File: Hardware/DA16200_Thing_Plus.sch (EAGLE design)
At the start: 61 parts, among them J1 MICRO-SDFRICTION, J2 THING_PLUS, J3 Qwiic, J5 USB C, J6 microSD, J7 CORTEX_JTAG_DEBUG_PTH_NS, Q1 20V/4.2A/52mΩ/1.4W, U1 DA16200MOD, U2 CH340E_MSOP10, U3 MCP73831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

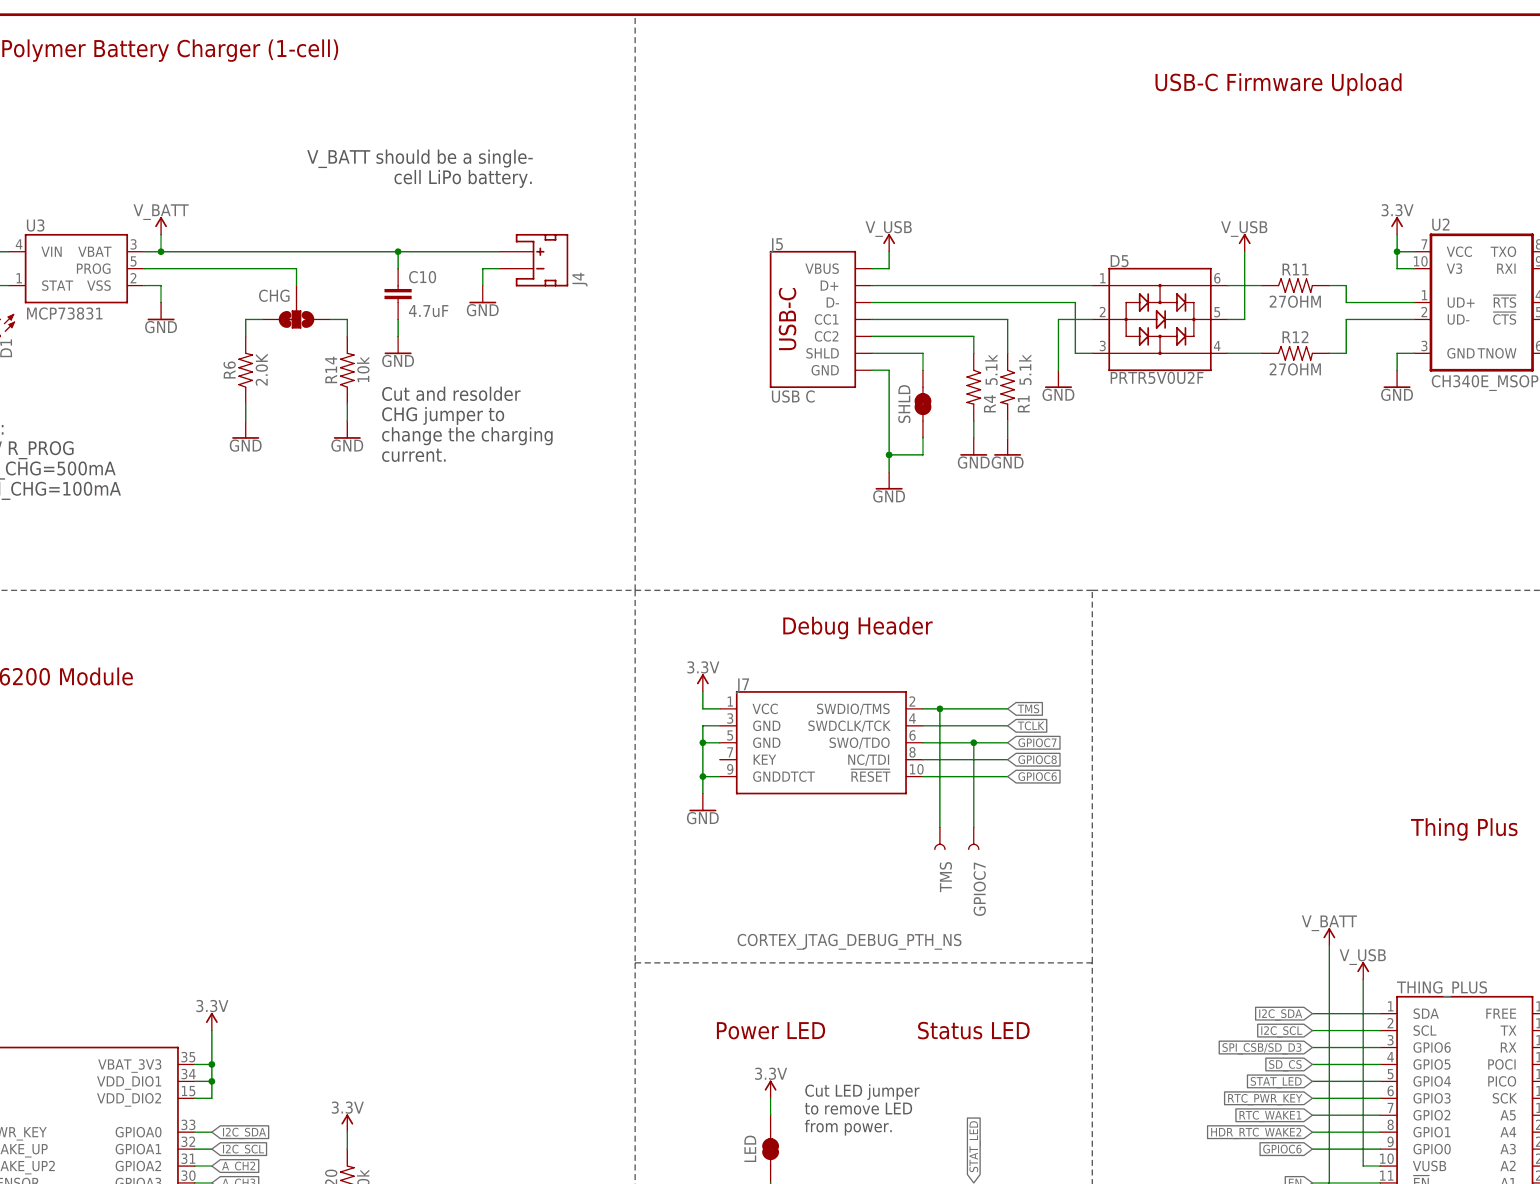
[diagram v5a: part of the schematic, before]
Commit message: Add jumper to remove 3.3V from CH340E
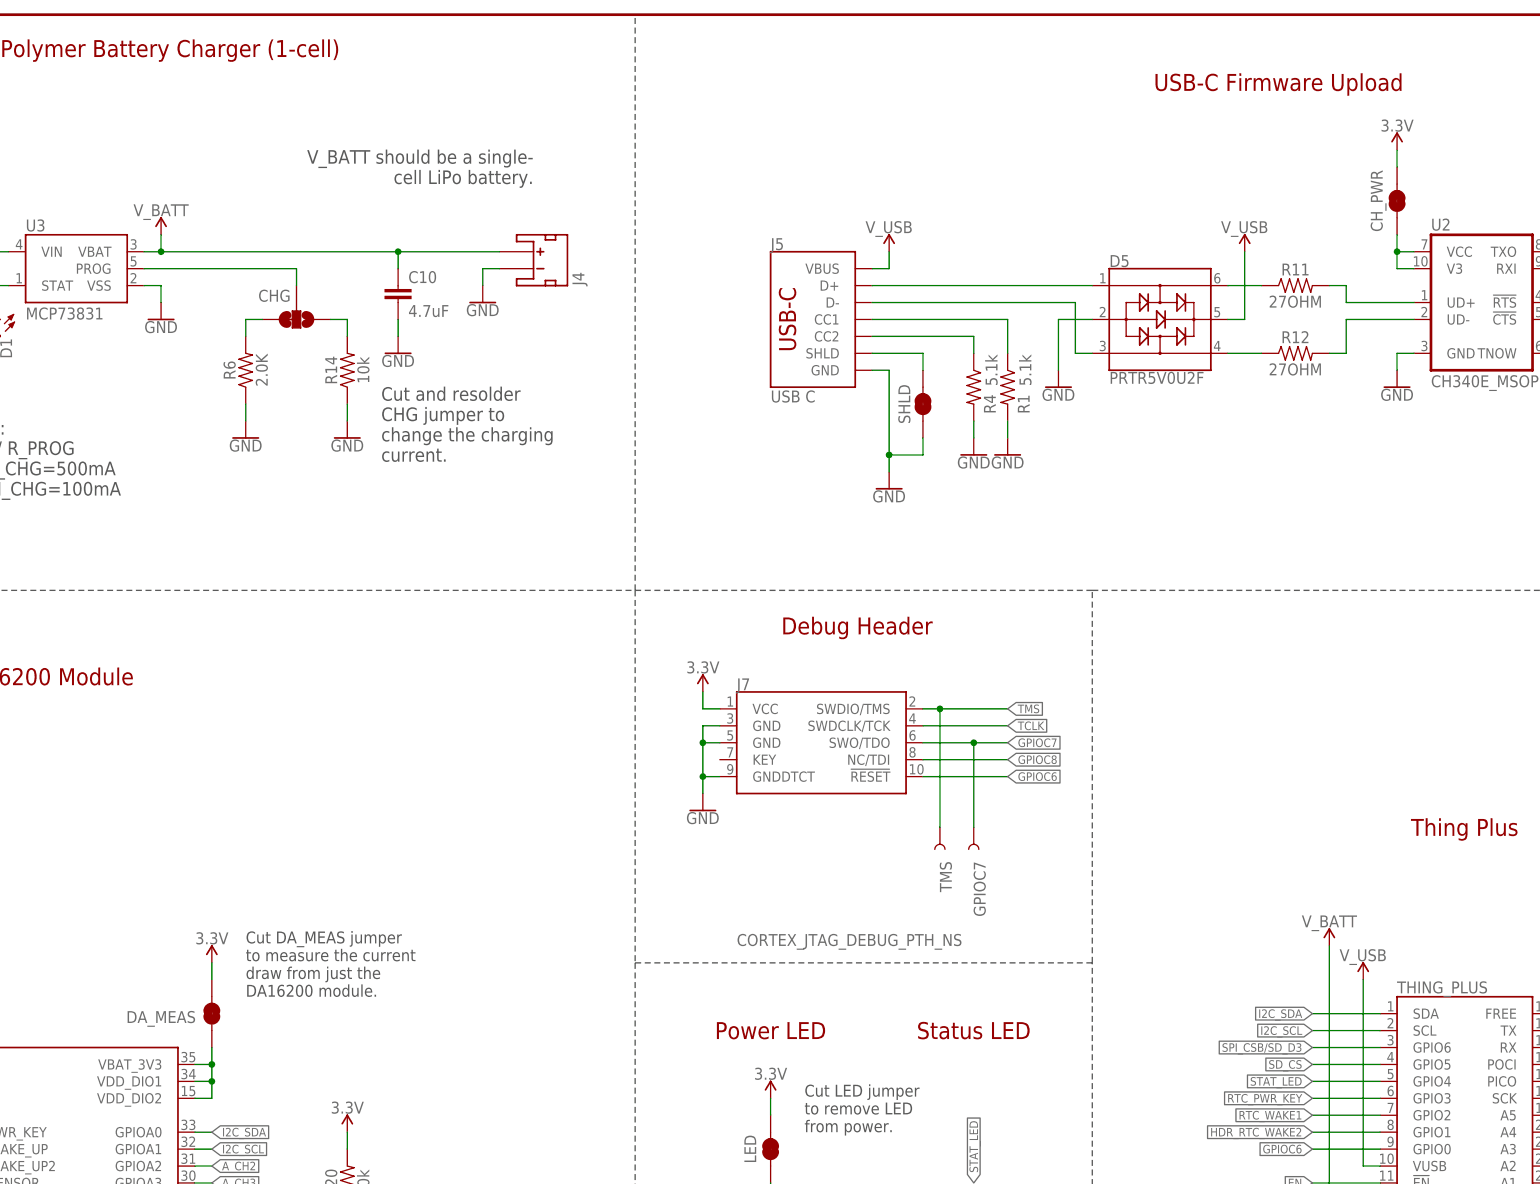
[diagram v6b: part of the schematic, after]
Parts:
- added CH_PWR, DA_MEAS: JUMPER-SMT_2_NC_TRACE_SILK, SparkFun-Jumpers:JUMPER-SMT_2_NC_TRACE_SILK
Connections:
- new net N$25: DA_MEAS.1, U1.VBAT_3V3, U1.VDD_DIO1, U1.VDD_DIO2
- new net N$26: CH_PWR.1, U2.V3, U2.VCC
- net 3.3V: now also CH_PWR.2, DA_MEAS.2; no longer U1.VBAT_3V3, U1.VDD_DIO1, U1.VDD_DIO2, U2.V3, U2.VCC
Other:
- note added: "Cut DA_MEAS jumper to measure the current draw from just the DA16200 module."
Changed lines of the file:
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@@
 <part name="J1" library="SparkFun-Connectors" deviceset="MICRO-SD" device="FRICTION"/>
 <part name="CHG_LED" library="SparkFun-Jumpers" deviceset="JUMPER-SMT_2_NC_TRACE" device="_SILK" package3d_urn="urn:adsk.eagle:package:39281/1"/>
+<part name="DA_MEAS" library="SparkFun-Jumpers" deviceset="JUMPER-SMT_2_NC_TRACE" device="_SILK" package3d_urn="urn:adsk.eagle:package:39281/1"/>
+<part name="CH_PWR" library="SparkFun-Jumpers" deviceset="JUMPER-SMT_2_NC_TRACE" device="_SILK" package3d_urn="urn:adsk.eagle:package:39281/1"/>
 </parts>
 <sheets>
@@
 to GND and enter sleep mode 1. Refer
 to the datasheet for more information.</text>
+<text x="203.2" y="132.08" size="1.778" layer="97" font="vector">Cut DA_MEAS jumper
+to measure the current
+draw from just the
+DA16200 module.</text>
 </plain>
 <instances>
@@
 <attribute name="VALUE" x="157.48" y="59.69" size="1.778" layer="96" align="top-left"/>
 </instance>
-<instance part="SUPPLY5" gate="G$1" x="198.12" y="127" smashed="yes">
-<attribute name="VALUE" x="198.12" y="129.794" size="1.778" layer="96" align="bottom-center"/>
+<instance part="SUPPLY5" gate="G$1" x="198.12" y="137.16" smashed="yes">
+<attribute name="VALUE" x="198.12" y="139.954" size="1.778" layer="96" align="bottom-center"/>
 </instance>
 <instance part="GND3" gate="1" x="198.12" y="55.88" smashed="yes">
@@
 <attribute name="VALUE" x="375.92" y="223.266" size="1.778" layer="96" align="top-center"/>
 </instance>
-<instance part="SUPPLY11" gate="G$1" x="375.92" y="246.38" smashed="yes">
-<attribute name="VALUE" x="375.92" y="249.174" size="1.778" layer="96" align="bottom-center"/>
+<instance part="SUPPLY11" gate="G$1" x="375.92" y="259.08" smashed="yes">
+<attribute name="VALUE" x="375.92" y="261.874" size="1.778" layer="96" align="bottom-center"/>
 </instance>
 <instance part="C1" gate="G$1" x="421.64" y="236.22" smashed="yes">
@@
 <instance part="CHG_LED" gate="G$1" x="147.32" y="233.68" smashed="yes" rot="R90">
 <attribute name="NAME" x="144.272" y="233.68" size="1.778" layer="95" font="vector" rot="R90" align="center"/>
+</instance>
+<instance part="DA_MEAS" gate="G$1" x="198.12" y="129.54" smashed="yes" rot="R90">
+<attribute name="NAME" x="190.5" y="129.032" size="1.778" layer="95" font="vector" rot="R180" align="center"/>
+</instance>
+<instance part="CH_PWR" gate="G$1" x="375.92" y="251.46" smashed="yes" rot="R90">
+<attribute name="NAME" x="372.872" y="251.46" size="1.778" layer="95" font="vector" rot="R90" align="center"/>
 </instance>
 </instances>
@@
 </segment>
 <segment>
-<pinref part="U1" gate="G$1" pin="VDD_DIO2"/>
-<wire x1="195.58" y1="116.84" x2="198.12" y2="116.84" width="0.1524" layer="91"/>
-<wire x1="198.12" y1="116.84" x2="198.12" y2="119.38" width="0.1524" layer="91"/>
-<pinref part="U1" gate="G$1" pin="VBAT_3V3"/>
-<wire x1="198.12" y1="119.38" x2="198.12" y2="121.92" width="0.1524" layer="91"/>
-<wire x1="198.12" y1="121.92" x2="198.12" y2="127" width="0.1524" layer="91"/>
-<wire x1="195.58" y1="121.92" x2="198.12" y2="121.92" width="0.1524" layer="91"/>
-<junction x="198.12" y="121.92"/>
-<pinref part="U1" gate="G$1" pin="VDD_DIO1"/>
-<wire x1="195.58" y1="119.38" x2="198.12" y2="119.38" width="0.1524" layer="91"/>
-<junction x="198.12" y="119.38"/>
-<pinref part="SUPPLY5" gate="G$1" pin="3.3V"/>
-</segment>
-<segment>
 <pinref part="J2" gate="G$1" pin="3V3"/>
 <wire x1="398.78" y1="93.98" x2="401.32" y2="93.98" width="0.1524" layer="91"/>
@@
 </segment>
 <segment>
-<pinref part="U2" gate="U1" pin="V3"/>
-<wire x1="378.46" y1="241.3" x2="375.92" y2="241.3" width="0.1524" layer="91"/>
-<wire x1="375.92" y1="241.3" x2="375.92" y2="243.84" width="0.1524" layer="91"/>
-<pinref part="U2" gate="U1" pin="VCC"/>
-<wire x1="375.92" y1="243.84" x2="375.92" y2="246.38" width="0.1524" layer="91"/>
-<wire x1="378.46" y1="243.84" x2="375.92" y2="243.84" width="0.1524" layer="91"/>
-<junction x="375.92" y="243.84"/>
-<pinref part="SUPPLY11" gate="G$1" pin="3.3V"/>
-</segment>
-<segment>
 <pinref part="C1" gate="G$1" pin="1"/>
 <pinref part="SUPPLY12" gate="G$1" pin="3.3V"/>
@@
 <wire x1="101.6" y1="58.42" x2="101.6" y2="60.96" width="0.1524" layer="91"/>
 <pinref part="SUPPLY2" gate="G$1" pin="3.3V"/>
+</segment>
+<segment>
+<pinref part="SUPPLY5" gate="G$1" pin="3.3V"/>
+<pinref part="DA_MEAS" gate="G$1" pin="2"/>
+<wire x1="198.12" y1="137.16" x2="198.12" y2="134.62" width="0.1524" layer="91"/>
+</segment>
+<segment>
+<pinref part="CH_PWR" gate="G$1" pin="2"/>
+<pinref part="SUPPLY11" gate="G$1" pin="3.3V"/>
+<wire x1="375.92" y1="256.54" x2="375.92" y2="259.08" width="0.1524" layer="91"/>
 </segment>
 </net>
@@
 </segment>
 </net>
+<net name="N$25" class="0">
+<segment>
+<pinref part="U1" gate="G$1" pin="VDD_DIO2"/>
+<wire x1="195.58" y1="116.84" x2="198.12" y2="116.84" width="0.1524" layer="91"/>
+<wire x1="198.12" y1="116.84" x2="198.12" y2="119.38" width="0.1524" layer="91"/>
+<pinref part="U1" gate="G$1" pin="VBAT_3V3"/>
+<wire x1="198.12" y1="119.38" x2="198.12" y2="121.92" width="0.1524" layer="91"/>
+<wire x1="195.58" y1="121.92" x2="198.12" y2="121.92" width="0.1524" layer="91"/>
+<pinref part="U1" gate="G$1" pin="VDD_DIO1"/>
+<wire x1="195.58" y1="119.38" x2="198.12" y2="119.38" width="0.1524" layer="91"/>
+<junction x="198.12" y="119.38"/>
+<pinref part="DA_MEAS" gate="G$1" pin="1"/>
+<wire x1="198.12" y1="124.46" x2="198.12" y2="121.92" width="0.1524" layer="91"/>
+<junction x="198.12" y="121.92"/>
+</segment>
+</net>
+<net name="N$26" class="0">
+<segment>
+<pinref part="U2" gate="U1" pin="V3"/>
+<wire x1="378.46" y1="241.3" x2="375.92" y2="241.3" width="0.1524" layer="91"/>
+<wire x1="375.92" y1="241.3" x2="375.92" y2="243.84" width="0.1524" layer="91"/>
+<pinref part="U2" gate="U1" pin="VCC"/>
+<wire x1="378.46" y1="243.84" x2="375.92" y2="243.84" width="0.1524" layer="91"/>
+<pinref part="CH_PWR" gate="G$1" pin="1"/>
+<wire x1="375.92" y1="246.38" x2="375.92" y2="243.84" width="0.1524" layer="91"/>
+<junction x="375.92" y="243.84"/>
+</segment>
+</net>

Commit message: Remove SD card socket from design
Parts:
- removed C2: 0.1uF, SparkFun-Capacitors:0.1UF-0402T-16V-10%
- removed J1: MICRO-SDFRICTION, SparkFun-Connectors:MICRO-SDFRICTION
- removed J6: microSD, SparkFun-Connectors:MICRO-SD-SDIOPUSH-PUSH
- removed R21: 10k, SparkFun-Resistors:10KOHM-0402T-1/16W-1%
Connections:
- removed net !RESET!/SPI_CLK/SD_D2: J1.DAT2, J2.!RESET, J2.SCK, J6.CLK/SCK, R13.2, U1.GPIOA7
- removed net SPI_CSB/SD_D3: J1.DAT3/!CS!, J2.GPIO6, R20.1, U1.GPIOA6
- removed net SPI_PICO/SD_D1: J1.DAT1, J2.PICO, J6.CMD/SDI, U1.GPIOA8
- removed net SPI_POCI/SD_D0: J1.DAT0/SDO, J2.POCI, J6.DAT0/SDO, U1.GPIOA9
- removed net U1RXI/SD_CLK: J1.CLK/SCK, J2.RX, U1.GPIOA5
- removed net U1TXO/SD_CMD: J1.CMD/SDI, J2.TX, U1.GPIOA4
- new net !RESET!/SPI_CLK: J2.!RESET, J2.SCK, R13.2, U1.GPIOA7
- new net SPI_CSB: J2.GPIO6, R20.1, U1.GPIOA6
- new net SPI_PICO: J2.PICO, U1.GPIOA8
- new net SPI_POCI: J2.POCI, U1.GPIOA9
- new net U1RXI: J2.RX, U1.GPIOA5
- new net U1TXO: J2.TX, U1.GPIOA4
- net 3.3V: no longer C2.1, J1.VCC, R21.2
- net GND: no longer C2.2, J1.GND
- net SD_CS: no longer J6.DAT3/!CS!, R21.1
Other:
- note added: "v10"
- note removed: "uSD Socket"
- note removed: "v01"
- moved on the sheet: I2C_PU, J3, R10, R17

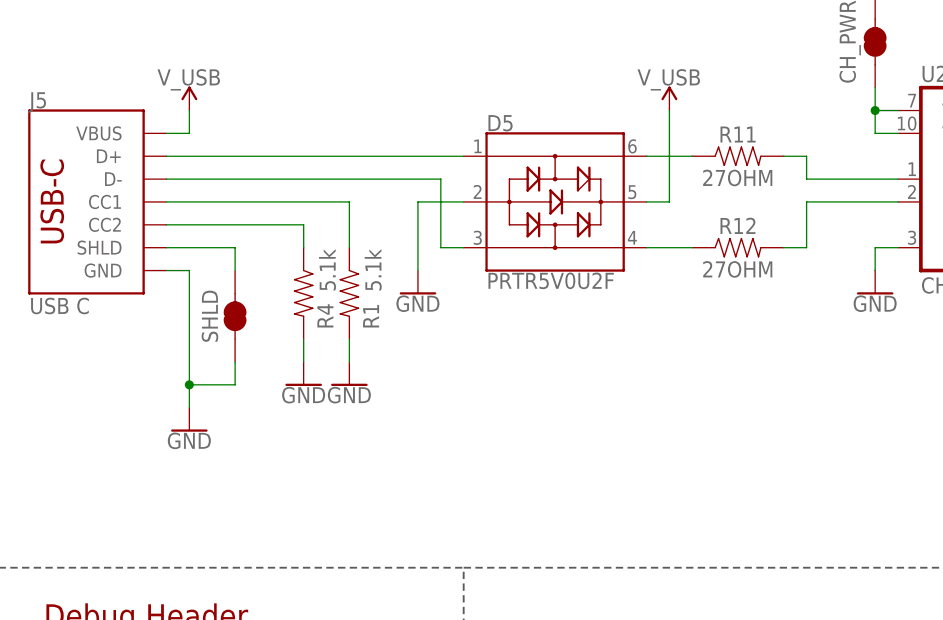
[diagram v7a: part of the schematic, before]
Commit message: Design review updates
Schematic:
* Remove "Ohm" from R11/R12 value
* Add schematic symbol for ground onto USB SHLD
Board:
* set layers in order
* Fix polygons to line up in DA16200 keep out area
* Add vias to stitch GND
* Fix some acid traps
* Evenly space out some traces
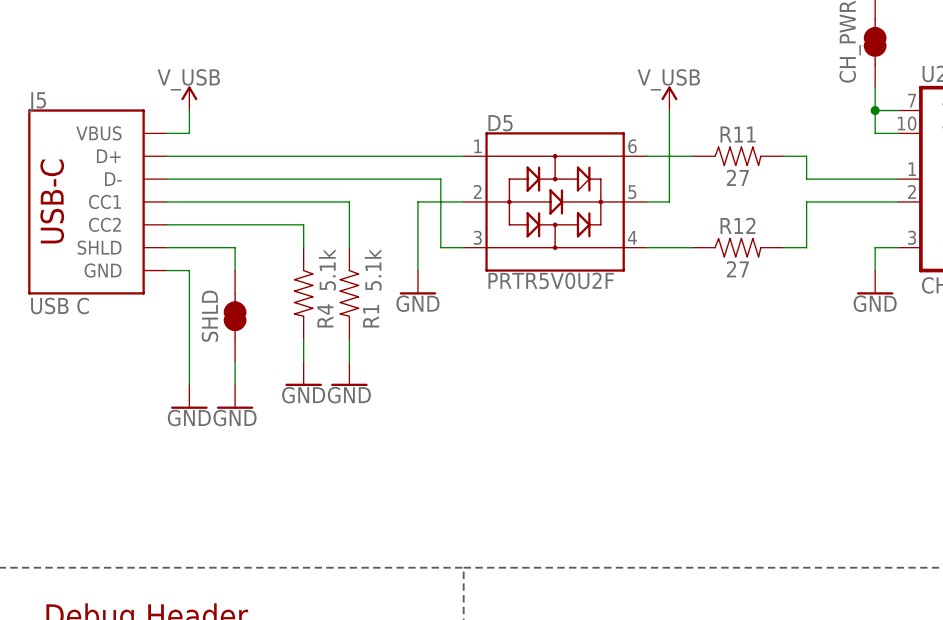
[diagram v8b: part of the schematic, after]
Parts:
- R11, R12: value 27OHM -> 27
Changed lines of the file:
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@@
 <part name="D5" library="SparkFun-IC-Power" deviceset="PRTR5V0U2" device="F"/>
 <part name="GND20" library="SparkFun-PowerSymbols" deviceset="GND" device=""/>
-<part name="R11" library="SparkFun-Resistors" deviceset="27OHM" device="" value="27OHM"/>
-<part name="R12" library="SparkFun-Resistors" deviceset="27OHM" device="" value="27OHM"/>
+<part name="R11" library="SparkFun-Resistors" deviceset="27OHM" device="" value="27"/>
+<part name="R12" library="SparkFun-Resistors" deviceset="27OHM" device="" value="27"/>
 <part name="SUPPLY14" library="SparkFun-PowerSymbols" deviceset="V_USB" device=""/>
 <part name="R13" library="SparkFun-Resistors" deviceset="200OHM" device="-0402T-1/16W-1%" value="200"/>
@@
 <part name="DA_MEAS" library="SparkFun-Jumpers" deviceset="JUMPER-SMT_2_NC_TRACE" device="_SILK" package3d_urn="urn:adsk.eagle:package:39281/1"/>
 <part name="CH_PWR" library="SparkFun-Jumpers" deviceset="JUMPER-SMT_2_NC_TRACE" device="_SILK" package3d_urn="urn:adsk.eagle:package:39281/1"/>
+<part name="GND2" library="SparkFun-PowerSymbols" deviceset="GND" device=""/>
 </parts>
 <sheets>
@@
 <attribute name="VALUE" x="238.76" y="235.966" size="1.778" layer="96" align="top-center"/>
 </instance>
-<instance part="GND8" gate="1" x="299.72" y="208.28" smashed="yes">
-<attribute name="VALUE" x="299.72" y="208.026" size="1.778" layer="96" align="top-center"/>
+<instance part="GND8" gate="1" x="299.72" y="210.82" smashed="yes">
+<attribute name="VALUE" x="299.72" y="210.566" size="1.778" layer="96" align="top-center"/>
 </instance>
 <instance part="GND7" gate="1" x="312.42" y="76.2" smashed="yes">
@@
 <instance part="CH_PWR" gate="G$1" x="375.92" y="251.46" smashed="yes" rot="R90">
 <attribute name="NAME" x="372.872" y="251.46" size="1.778" layer="95" font="vector" rot="R90" align="center"/>
+</instance>
+<instance part="GND2" gate="1" x="304.8" y="210.82" smashed="yes">
+<attribute name="VALUE" x="304.8" y="210.566" size="1.778" layer="96" align="top-center"/>
 </instance>
 </instances>
@@
 <segment>
 <wire x1="299.72" y1="226.06" x2="299.72" y2="213.36" width="0.1524" layer="91"/>
-<wire x1="299.72" y1="213.36" x2="299.72" y2="210.82" width="0.1524" layer="91"/>
 <wire x1="299.72" y1="226.06" x2="297.18" y2="226.06" width="0.1524" layer="91"/>
 <pinref part="J5" gate="J1" pin="GND"/>
 <pinref part="GND8" gate="1" pin="GND"/>
-<pinref part="SHLD" gate="G$1" pin="1"/>
-<wire x1="304.8" y1="215.9" x2="304.8" y2="213.36" width="0.1524" layer="91"/>
-<wire x1="304.8" y1="213.36" x2="299.72" y2="213.36" width="0.1524" layer="91"/>
-<junction x="299.72" y="213.36"/>
 </segment>
 <segment>
@@
 <pinref part="GND17" gate="1" pin="GND"/>
 </segment>
+<segment>
+<pinref part="SHLD" gate="G$1" pin="1"/>
+<wire x1="304.8" y1="215.9" x2="304.8" y2="213.36" width="0.1524" layer="91"/>
+<pinref part="GND2" gate="1" pin="GND"/>
+</segment>
 </net>
